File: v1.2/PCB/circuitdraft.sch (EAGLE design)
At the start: 23 parts, among them Y1 CY16BPS

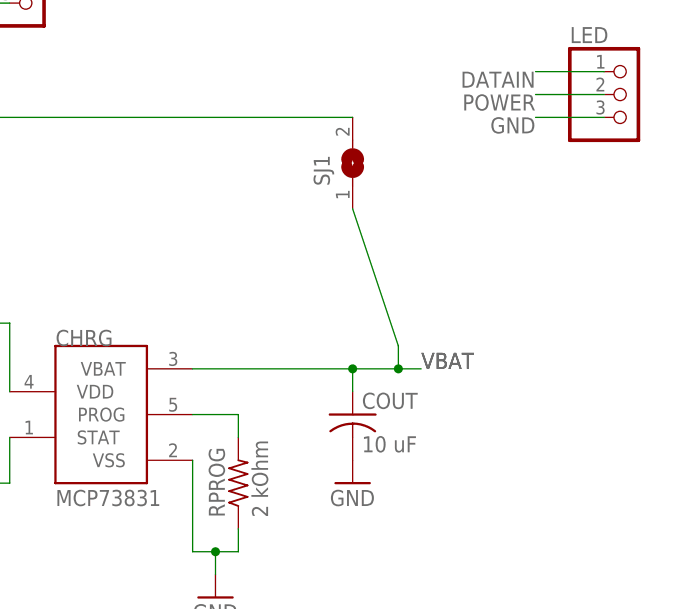
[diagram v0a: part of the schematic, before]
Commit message: Added switch. Passes DRC
Final 1.2
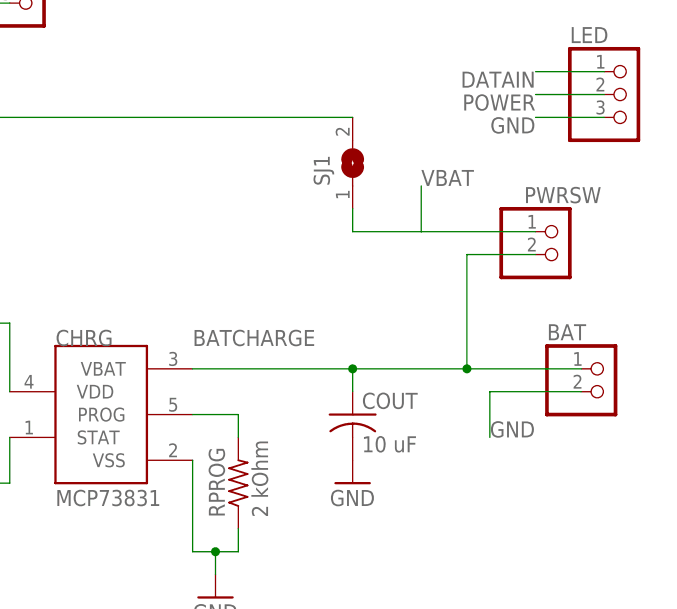
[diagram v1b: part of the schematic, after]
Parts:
- added BAT, PWRSW: (no value), pinhead:PINHD-1X2
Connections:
- new net BATCHARGE: BAT.1, CHRG.VBAT, COUT.1, PWRSW.2
- net GND: now also BAT.2
- net VBAT: now also PWRSW.1; no longer CHRG.VBAT, COUT.1
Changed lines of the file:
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@@
 <part name="RPROG" library="3DPC" deviceset="R-US_" device="R0603" package3d_urn="urn:adsk.eagle:package:23555/3" value="2 kOhm"/>
 <part name="SJ1" library="jumper" library_urn="urn:adsk.eagle:library:252" deviceset="SJ" device="" package3d_urn="urn:adsk.eagle:package:15471/1"/>
+<part name="BAT" library="pinhead" library_urn="urn:adsk.eagle:library:325" deviceset="PINHD-1X2" device="" package3d_urn="urn:adsk.eagle:package:22435/2"/>
+<part name="PWRSW" library="pinhead" library_urn="urn:adsk.eagle:library:325" deviceset="PINHD-1X2" device="" package3d_urn="urn:adsk.eagle:package:22435/2"/>
 </parts>
 <sheets>
@@
 <attribute name="NAME" x="266.7" y="96.52" size="1.778" layer="95" rot="R90"/>
 <attribute name="VALUE" x="273.05" y="96.52" size="1.778" layer="96" rot="R90"/>
+</instance>
+<instance part="BAT" gate="G$1" x="297.18" y="73.66" smashed="yes">
+<attribute name="NAME" x="290.83" y="79.375" size="1.778" layer="95"/>
+<attribute name="VALUE" x="290.83" y="68.58" size="1.778" layer="96"/>
+</instance>
+<instance part="PWRSW" gate="G$1" x="292.1" y="88.9" smashed="yes">
+<attribute name="NAME" x="288.29" y="94.615" size="1.778" layer="95"/>
+<attribute name="VALUE" x="285.75" y="83.82" size="1.778" layer="96"/>
 </instance>
 </instances>
@@
 <junction x="254" y="55.88"/>
 </segment>
+<segment>
+<pinref part="BAT" gate="G$1" pin="2"/>
+<wire x1="294.64" y1="73.66" x2="284.48" y2="73.66" width="0.1524" layer="91"/>
+<wire x1="284.48" y1="73.66" x2="284.48" y2="68.58" width="0.1524" layer="91"/>
+<label x="284.48" y="68.58" size="1.778" layer="95"/>
+</segment>
 </net>
 <net name="INTERRUPT" class="0">
@@
 </segment>
 <segment>
-<pinref part="CHRG" gate="G$1" pin="VBAT"/>
-<wire x1="251.46" y1="76.2" x2="269.24" y2="76.2" width="0.1524" layer="91"/>
-<wire x1="269.24" y1="76.2" x2="274.32" y2="76.2" width="0.1524" layer="91"/>
-<pinref part="COUT" gate="G$1" pin="1"/>
-<wire x1="274.32" y1="76.2" x2="276.86" y2="76.2" width="0.1524" layer="91"/>
-<wire x1="269.24" y1="73.66" x2="269.24" y2="76.2" width="0.1524" layer="91"/>
-<junction x="269.24" y="76.2"/>
-<label x="276.86" y="76.2" size="1.778" layer="95"/>
-<label x="276.86" y="76.2" size="1.778" layer="95"/>
+<pinref part="PWRSW" gate="G$1" pin="1"/>
+<wire x1="289.56" y1="91.44" x2="276.86" y2="91.44" width="0.1524" layer="91"/>
+<wire x1="276.86" y1="91.44" x2="276.86" y2="96.52" width="0.1524" layer="91"/>
+<label x="276.86" y="96.52" size="1.778" layer="95"/>
 <pinref part="SJ1" gate="1" pin="1"/>
-<wire x1="274.32" y1="76.2" x2="274.32" y2="78.74" width="0.1524" layer="91"/>
-<wire x1="274.32" y1="78.74" x2="269.24" y2="93.98" width="0.1524" layer="91"/>
-<junction x="274.32" y="76.2"/>
+<wire x1="269.24" y1="93.98" x2="269.24" y2="91.44" width="0.1524" layer="91"/>
+<wire x1="269.24" y1="91.44" x2="276.86" y2="91.44" width="0.1524" layer="91"/>
 </segment>
 </net>
@@
 </segment>
 </net>
+<net name="BATCHARGE" class="1">
+<segment>
+<pinref part="CHRG" gate="G$1" pin="VBAT"/>
+<wire x1="251.46" y1="76.2" x2="269.24" y2="76.2" width="0.1524" layer="91"/>
+<pinref part="COUT" gate="G$1" pin="1"/>
+<wire x1="269.24" y1="73.66" x2="269.24" y2="76.2" width="0.1524" layer="91"/>
+<junction x="269.24" y="76.2"/>
+<pinref part="BAT" gate="G$1" pin="1"/>
+<wire x1="294.64" y1="76.2" x2="281.94" y2="76.2" width="0.1524" layer="91"/>
+<pinref part="PWRSW" gate="G$1" pin="2"/>
+<wire x1="281.94" y1="76.2" x2="269.24" y2="76.2" width="0.1524" layer="91"/>
+<wire x1="289.56" y1="88.9" x2="281.94" y2="88.9" width="0.1524" layer="91"/>
+<wire x1="281.94" y1="88.9" x2="281.94" y2="76.2" width="0.1524" layer="91"/>
+<junction x="281.94" y="76.2"/>
+<label x="251.46" y="78.74" size="1.778" layer="95"/>
+</segment>
+</net>
